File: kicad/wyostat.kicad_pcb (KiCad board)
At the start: 2 copper layers, 75 parts, among them J1 PWR_In, J10 MOSI, J11 RST, J12 GND, J13 AC_IN, J14 ~RST, J15 AC_IN, J16 5V_SEL, J2 OUT1, J3 OUT2, J4 OUT3, J5 I2C_ext1, J6 MISO, J7 3V3, J8 SCK, J9 SPI, Q1 BT136-600, Q2 BT136-600, Q3 BT136-600, U1 MOC3063M, U2 MOC3063M, U3 MOC3063M, U4 Wemos-Lolin, U5 MAX17502FATB+T, U6 Converter_AC_DC

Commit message: kicad PCB, WIP
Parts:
- removed J14: ~RST, wyostat_fp:Pin_Header_Straight_1x01
- moved R16 143.6 mm to (38.7, 134.6), turned to 90 degrees
- moved R7 127.3 mm to (55.2, 120.7), turned to 90 degrees
- moved R3 122.3 mm to (36.2, 109.9), turned to 90 degrees
- moved R10 119.5 mm to (38.7, 124.5), turned to 90 degrees
- moved U3 116.5 mm to (47.0, 132.7), turned to 270 degrees
- moved R11 111.1 mm to (80.0, 122.6)
- moved R8 110.3 mm to (55.2, 124.5), turned to 90 degrees
- moved R9 109.9 mm to (36.2, 120.0), turned to 90 degrees
- moved J10 108.2 mm to (56.5, 85.7), turned to 270 degrees
- moved J11 105.9 mm to (46.4, 88.3), turned to 90 degrees
- moved C1 105.3 mm to (85.1, 112.4), turned to 90 degrees
- moved R13 104.5 mm to (55.2, 130.8), turned to 90 degrees
- moved C5 104.5 mm to (85.1, 132.7), turned to 90 degrees
- moved D1 103.3 mm to (38.7, 109.9), turned to 90 degrees
- moved JP1 96.6 mm to (36.2, 114.3), turned to 90 degrees
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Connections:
- J13 pad 1: Net-(F1-Pad2) -> Net-(D4-Pad3)
- J13 pad 2: Net-(D4-Pad3) -> Net-(F1-Pad2)
- U4 pad 1: Net-(U4-Pad1) -> (no net)
- U4 pad 11: Net-(U4-Pad11) -> (no net)
- U4 pad 12: Net-(U4-Pad12) -> (no net)
- U4 pad 20: Net-(U4-Pad20) -> (no net)
- U4 pad 21: Net-(U4-Pad21) -> (no net)
- U4 pad 22: Net-(U4-Pad22) -> (no net)
- U4 pad 23: Net-(U4-Pad23) -> (no net)
- U4 pad 26: Net-(U4-Pad26) -> (no net)
- U4 pad 5: Net-(U4-Pad5) -> (no net)
- U4 pad 6: Net-(U4-Pad6) -> (no net)
- U5 pad 7: Net-(U5-Pad7) -> (no net)
- U5 pad 8: Net-(J14-Pad1) -> (no net)

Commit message: layou, WIP
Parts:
- added JP4: GND, wyostat_fp:LED_0402, F.Cu at (71.0, 70.2)
- added SC1: SCREW, wyostat_fp:MountingHole_3.2mm_M3_Pad_Via, F.Cu at (36.8, 36.8)
- added SC2: SCREW, wyostat_fp:MountingHole_3.2mm_M3_Pad_Via, F.Cu at (125.7, 36.8)
- added SC3: SCREW, wyostat_fp:MountingHole_3.2mm_M3_Pad_Via, F.Cu at (36.8, 125.7)
- added SC4: SCREW, wyostat_fp:MountingHole_3.2mm_M3_Pad_Via, F.Cu at (125.7, 125.7)
- U1, U2, U3: footprint wyostat_fp:Optocoupler_6pin -> wyostat_fp:Optocoupler_6pin_smd
- U6: footprint wyostat_fp:Converter_AC_DC -> wyostat_fp:Converter_AC_DC_Eshion
- moved J16 68.3 mm to (50.8, 74.3), turned to 180 degrees
- moved S4 59.3 mm to (109.9, 46.4)
- moved S2 59.3 mm to (117.5, 38.7), turned to 270 degrees
- moved S3 55.7 mm to (117.5, 54.0), turned to 270 degrees
- moved S1 55.7 mm to (125.1, 46.4), turned to 270 degrees
- moved C9 36.4 mm to (85.7, 68.6), turned to 270 degrees
- moved U6 34.8 mm to (70.9, 118.2), turned to 180 degrees
- moved C13 34.6 mm to (70.9, 63.8), turned to 0 degrees
- moved C10 34.4 mm to (78.7, 68.6)
- moved D3 33.8 mm to (53.3, 99.7)
- moved R15 33.8 mm to (50.8, 99.7)
- moved C4 33.8 mm to (77.5, 92.1)
- moved C6 33.8 mm to (77.5, 102.2)
- moved D1 33.8 mm to (53.3, 79.4)
- moved D2 33.8 mm to (53.3, 89.5)
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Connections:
- net Net-(C10-Pad1) renamed /40VDC
- net Net-(C12-Pad1) renamed /VCC
- net Net-(C13-Pad1) renamed /SS
- net Net-(L1-Pad1) renamed /LX
- C1 pad 1: /OUT1 -> /LINE
- C11 pad 2: GND -> GNDREF
- C14 pad 2: GND -> GNDREF
- C2 pad 2: /NEUT -> /OUT1
- C3 pad 1: /OUT2 -> /LINE
- C4 pad 2: /NEUT -> /OUT2
- C5 pad 1: /OUT3 -> /LINE
- C6 pad 2: /NEUT -> /OUT3
- J13 pad 1: Net-(D4-Pad3) -> Net-(F1-Pad2)
- J13 pad 2: Net-(F1-Pad2) -> Net-(D4-Pad3)
- J2 pad 1: /LINE -> /OUT1
- J2 pad 2: /OUT1 -> /NEUT
- J3 pad 1: /LINE -> /OUT2
- J3 pad 2: /OUT2 -> /NEUT
- J4 pad 1: /LINE -> /OUT3
- J4 pad 2: /OUT3 -> /NEUT
- Q1 pad 1: /OUT1 -> /LINE
- Q1 pad 2: /NEUT -> /OUT1
- Q2 pad 1: /OUT2 -> /LINE
- Q2 pad 2: /NEUT -> /OUT2
- Q3 pad 1: /OUT3 -> /LINE
- Q3 pad 2: /NEUT -> /OUT3
- R11 pad 1: /NEUT -> /OUT2
- R12 pad 1: /NEUT -> /OUT2
- R14 pad 1: /OUT3 -> /LINE
- R17 pad 1: /NEUT -> /OUT3
- R18 pad 1: /NEUT -> /OUT3
- R2 pad 1: /OUT1 -> /LINE
- R5 pad 1: /NEUT -> /OUT1
- R6 pad 1: /NEUT -> /OUT1
- R8 pad 1: /OUT2 -> /LINE
- U4 pad 1: (no net) -> Net-(U4-Pad1)
- U4 pad 11: (no net) -> Net-(U4-Pad11)
- U4 pad 12: (no net) -> Net-(U4-Pad12)
- U4 pad 20: (no net) -> Net-(U4-Pad20)
- U4 pad 21: (no net) -> Net-(U4-Pad21)
- U4 pad 22: (no net) -> Net-(U4-Pad22)
- U4 pad 23: (no net) -> Net-(U4-Pad23)
- U4 pad 26: (no net) -> Net-(U4-Pad26)
- U4 pad 5: (no net) -> Net-(U4-Pad5)
- U4 pad 6: (no net) -> Net-(U4-Pad6)
- U5 pad 1: GND -> GNDREF
- U5 pad 7: (no net) -> Net-(U5-Pad7)
- U5 pad 8: (no net) -> /R
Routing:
- net GND: track 0.00 -> 29.8 mm
- net /40VDC: track 0.00 -> 26.1 mm
- net /3V3: track 0.00 -> 21.1 mm
- net /5V_IN1: track 0.00 -> 18.6 mm, vias 0 -> 2
- net Net-(D4-Pad3): track 0.00 -> 14.6 mm
- net /SW_M: track 0.00 -> 8.99 mm
- net /SW_I: track 0.00 -> 8.99 mm
- net /SW_D: track 0.00 -> 8.99 mm
- net Net-(F1-Pad2): track 0.00 -> 7.41 mm
- net Net-(D4-Pad4): track 0.00 -> 6.28 mm
- net GNDREF: track 0.00 -> 5.98 mm
- net /SS: track 0.00 -> 5.34 mm
- net /SW_E: track 0.00 -> 2.99 mm
- net /LX: track 0.00 -> 2.80 mm
- net /5V: track 0.00 -> 2.54 mm
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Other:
- board outline added: 99.1 x 99.1 mm

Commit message: kicad PCB, track layout
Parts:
- removed C7: 100nF, wyostat_fp:C_0805
- removed J10: MOSI, wyostat_fp:Pin_Header_Straight_1x01
- removed J11: RST, wyostat_fp:Pin_Header_Straight_1x01
- removed J12: GND, wyostat_fp:Pin_Header_Straight_1x01
- removed J6: MISO, wyostat_fp:Pin_Header_Straight_1x01
- removed J7: 3V3, wyostat_fp:Pin_Header_Straight_1x01
- removed J8: SCK, wyostat_fp:Pin_Header_Straight_1x01
- removed J9: SPI, wyostat_fp:Pin_Header_Straight_2x03
- moved C13 7.37 mm to (63.5, 63.9), turned to 180 degrees
- moved JP4 6.83 mm to (72.1, 63.5)
- moved R12 5.43 mm to (71.1, 88.9), turned to 180 degrees
- moved R17 5.43 mm to (71.1, 99.1), turned to 180 degrees
- moved R5 5.43 mm to (71.1, 78.7), turned to 180 degrees
- moved R1 2.29 mm to (71.1, 81.9), turned to 180 degrees
- moved R13 2.29 mm to (71.1, 102.2), turned to 180 degrees
- moved R7 2.29 mm to (71.1, 92.1), turned to 180 degrees
- moved C8 2.08 mm to (40.0, 52.7)
- moved R11 2.01 mm to (95.2, 90.2), turned to 90 degrees
- moved R18 2.01 mm to (95.2, 100.3), turned to 90 degrees
- moved R6 2.01 mm to (95.2, 80.0), turned to 90 degrees
- moved J5 1.90 mm to (36.8, 50.2)
- moved R2 1.80 mm to (71.1, 85.1), turned to 180 degrees
- moved R14 1.80 mm to (71.1, 105.4), turned to 180 degrees
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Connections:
- C11 pad 2: GNDREF -> GND
- C14 pad 2: GNDREF -> GND
- JP4 pad 2: GNDREF -> GND
- U1 pad 3: Net-(U1-Pad3) -> (no net)
- U1 pad 5: Net-(U1-Pad5) -> (no net)
- U2 pad 3: Net-(U2-Pad3) -> (no net)
- U2 pad 5: Net-(U2-Pad5) -> (no net)
- U3 pad 3: Net-(U3-Pad3) -> (no net)
- U3 pad 5: Net-(U3-Pad5) -> (no net)
- U4 pad 1: Net-(U4-Pad1) -> (no net)
- U4 pad 11: Net-(U4-Pad11) -> (no net)
- U4 pad 12: Net-(U4-Pad12) -> (no net)
- U4 pad 2: /IN1 -> /IN3
- U4 pad 20: Net-(U4-Pad20) -> (no net)
- U4 pad 21: Net-(U4-Pad21) -> (no net)
- U4 pad 22: Net-(U4-Pad22) -> (no net)
- U4 pad 23: Net-(U4-Pad23) -> (no net)
- U4 pad 24: /IN3 -> /IN1
- U4 pad 26: Net-(U4-Pad26) -> (no net)
- U4 pad 5: Net-(U4-Pad5) -> (no net)
- U4 pad 6: Net-(U4-Pad6) -> (no net)
- U5 pad 1: GNDREF -> GND
- U5 pad 7: Net-(U5-Pad7) -> (no net)
- U5 pad 8: /R -> (no net)
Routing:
- net /3V3: track 21.1 -> 180.6 mm
- net /LINE: track 0.00 -> 130.0 mm, vias 0 -> 3
- net GND: track 29.8 -> 129.3 mm, vias 0 -> 26
- net /IN3: track 0.00 -> 96.5 mm
- net /SW_E: track 2.99 -> 85.8 mm
- net /SW_D: track 8.99 -> 80.0 mm
- net /5V: track 2.54 -> 67.4 mm
- net /SW_I: track 8.99 -> 66.1 mm
- net /SW_M: track 8.99 -> 64.0 mm
- net /5V_IN2: track 0.00 -> 43.6 mm
- net /NEUT: track 0.00 -> 39.7 mm
- net /IN2: track 0.00 -> 39.6 mm
- net Net-(Q2-Pad3): track 0.00 -> 39.1 mm
- net Net-(Q3-Pad3): track 0.00 -> 39.1 mm
- net Net-(Q1-Pad3): track 0.00 -> 39.1 mm
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- added copper zone on F.Cu, net /40VDC
- added copper zone on F.Cu, net /5V_IN1
- added copper zone on F.Cu, net /LX
- added copper zone on B.Cu, net GND
- added copper zone on F.Cu, net GND
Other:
- net class 10mil added: clearance 0.2032, trace_width 0.254, via_dia 0.8128, via_drill 0.4064
- net class 15mil added: clearance 0.2032, trace_width 0.381, via_dia 0.8128, via_drill 0.4064
- net class 20mil added: clearance 0.2032, trace_width 0.508, via_dia 0.8128, via_drill 0.4064
- net class 30mil added: clearance 0.2032, trace_width 0.762, via_dia 0.8128, via_drill 0.4064
- net class 40mil added: clearance 0.2032, trace_width 1.016, via_dia 0.8128, via_drill 0.4064
- net class Default: clearance 0.2 -> 0.2032; trace_width 0.25 -> 0.254; via_dia 0.8 -> 0.8128; via_drill 0.4 -> 0.4064
- rule trace_clearance: 0.2 -> 0.2032

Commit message: initial board layout
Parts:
- removed F2: Polyfuse, wyostat_fp:Fuse_SMD2920
- removed J15: AC_IN, wyostat_fp:TerminalBlock_Pheonix_MPT-2.54mm_2pol
- added BT1: Batt_RTC, wyostat_fp:CR2032_SMD2, F.Cu at (42.5, 81.3)
- added C15: 4.7uF, wyostat_fp:C_0805, F.Cu at (95.9, 73.4)
- added C7: 100nF, wyostat_fp:C_0805, F.Cu at (40.0, 52.7)
- added D5: CDSOD323-T05L, Diodes_SMD:D_SOD-323_HandSoldering, F.Cu at (99.7, 74.3)
- added L2: 330E, wyostat_fp:R_0805, F.Cu at (99.7, 72.4)
- added L4: 330E, wyostat_fp:R_0805, F.Cu at (99.7, 64.8)
- added R23: 0E, wyostat_fp:R_0805, F.Cu at (99.7, 70.5)
- added R24: 0E, wyostat_fp:R_0805, F.Cu at (99.7, 68.6)
- added R25: 0E, wyostat_fp:R_0805, F.Cu at (99.7, 66.7)
- added R26: 10k, wyostat_fp:R_0805, F.Cu at (54.6, 76.2)
- added R27: 10k, wyostat_fp:R_0805, F.Cu at (54.6, 73.0)
- added R28: 4K7, wyostat_fp:R_0805, F.Cu at (54.6, 64.1)
- added R29: 4K7, wyostat_fp:R_0805, F.Cu at (54.6, 66.0)
- added TP1: ~RST, wyostat_fp:Pin_Header_Straight_1x01, F.Cu at (76.2, 68.6)
- added TP2: SQR, wyostat_fp:Pin_Header_Straight_1x01, F.Cu at (73.7, 68.6)
- added TP3: 32kHz, wyostat_fp:Pin_Header_Straight_1x01, F.Cu at (71.1, 68.6)
- J1: value PWR_In -> 24VAC IN
- J13: value AC_IN -> USB_microAB; footprint wyostat_fp:TerminalBlock_Pheonix_MPT-2.54mm_2pol -> wyostat_fp:USB_Micro-B_Molex-105017-0001
- J16: value 5V_SEL -> EXT<OFF>USB
- R14, R2, R8: value 470 -> 0E
- U6: value Converter_AC_DC -> DS3231N; footprint wyostat_fp:Converter_AC_DC_Eshion -> wyostat_fp:DS3231
- moved U6 50.4 mm to (62.2, 68.6), turned to 0 degrees
- moved J16 41.3 mm to (92.1, 72.4), turned to 270 degrees
- moved J1 27.9 mm to (106.7, 84.5)
- moved C8 21.6 mm to (54.6, 68.6), turned to 0 degrees
- moved R3 14.6 mm to (50.8, 94.0)
- moved JP1 13.3 mm to (50.8, 97.2)
- moved C10 12.7 mm to (78.7, 81.3)
- moved C11 12.7 mm to (71.0, 82.9)
- moved C12 12.7 mm to (70.9, 78.5)
- moved C13 12.7 mm to (63.5, 76.6)
- moved C14 12.7 mm to (67.3, 82.9)
- moved C3 12.7 mm to (99.7, 104.8)
- moved C4 12.7 mm to (77.5, 104.8)
- moved C5 12.7 mm to (99.7, 114.9)
- moved C6 12.7 mm to (77.5, 114.9)
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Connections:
- C1 pad 1: /LINE -> /24Vac-H
- C3 pad 1: /LINE -> /24Vac-H
- C5 pad 1: /LINE -> /24Vac-H
- C8 pad 1: /3V3 -> /rtc_ds3231/BAT
- D4 pad 3: Net-(D4-Pad3) -> /24Vac-C
- F1 pad 2: Net-(F1-Pad2) -> /24Vac-H
- J1 pad 1: /LINE -> /24Vac-H
- J1 pad 2: /NEUT -> /24Vac-C
- J13 pad 1: Net-(F1-Pad2) -> /USB+
- J13 pad 2: Net-(D4-Pad3) -> /D-
- J2 pad 2: /NEUT -> /24Vac-C
- J3 pad 2: /NEUT -> /24Vac-C
- J4 pad 2: /NEUT -> /24Vac-C
- Q1 pad 1: /LINE -> /24Vac-H
- Q2 pad 1: /LINE -> /24Vac-H
- Q3 pad 1: /LINE -> /24Vac-H
- R14 pad 1: /LINE -> /24Vac-H
- R2 pad 1: /LINE -> /24Vac-H
- R8 pad 1: /LINE -> /24Vac-H
- U6 pad 1: Net-(F2-Pad1) -> /rtc_ds3231/32kHz
- U6 pad 2: Net-(J15-Pad2) -> /3V3
- U6 pad 3: /5V_IN2 -> /rtc_ds3231/SQR
- U6 pad 4: GND -> /rtc_ds3231/RESET
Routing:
- net GND: track 129.3 -> 295.8 mm, vias 26 -> 32
- net /24Vac-H: track 0.00 -> 134.2 mm, vias 0 -> 4
- net /LINE: track 130.0 -> 0.00 mm, vias 3 -> 0
- net /3V3: track 180.6 -> 237.0 mm
- net /24Vac-C: track 0.00 -> 54.1 mm
- net /rtc_ds3231/BAT: track 0.00 -> 53.1 mm, vias 0 -> 3
- net /SCL: track 27.0 -> 71.6 mm, vias 0 -> 1
- net /SDA: track 31.2 -> 73.0 mm
- net /NEUT: track 39.7 -> 0.00 mm
- net /5V_IN2: track 43.6 -> 6.68 mm
- net /rtc_ds3231/SQR: track 0.00 -> 24.3 mm
- net Net-(J15-Pad2): track 24.0 -> 0.00 mm
- net Net-(J13-PadS1): track 0.00 -> 23.8 mm
- net /IN1: track 29.6 -> 52.5 mm, vias 0 -> 1
- net /5V_IN1: track 28.0 -> 47.4 mm, vias 2 -> 4
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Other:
- outline, holes or cut-outs redrawn
- board text added: "H | C"
- board text added: "SCL SDA 3V3 GND"

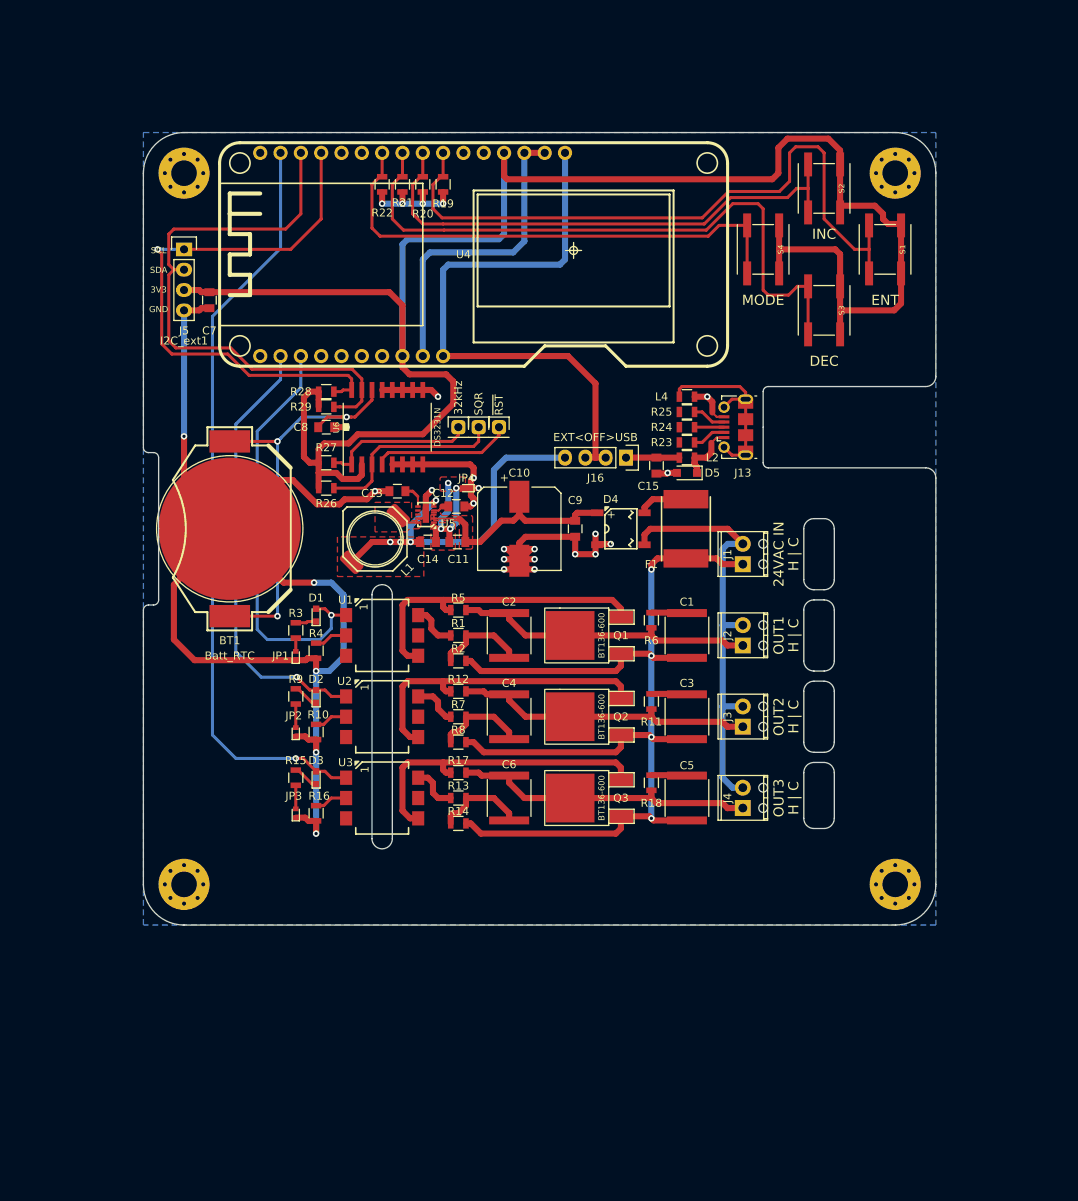
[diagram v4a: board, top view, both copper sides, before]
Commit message: adding pads for spring contacts
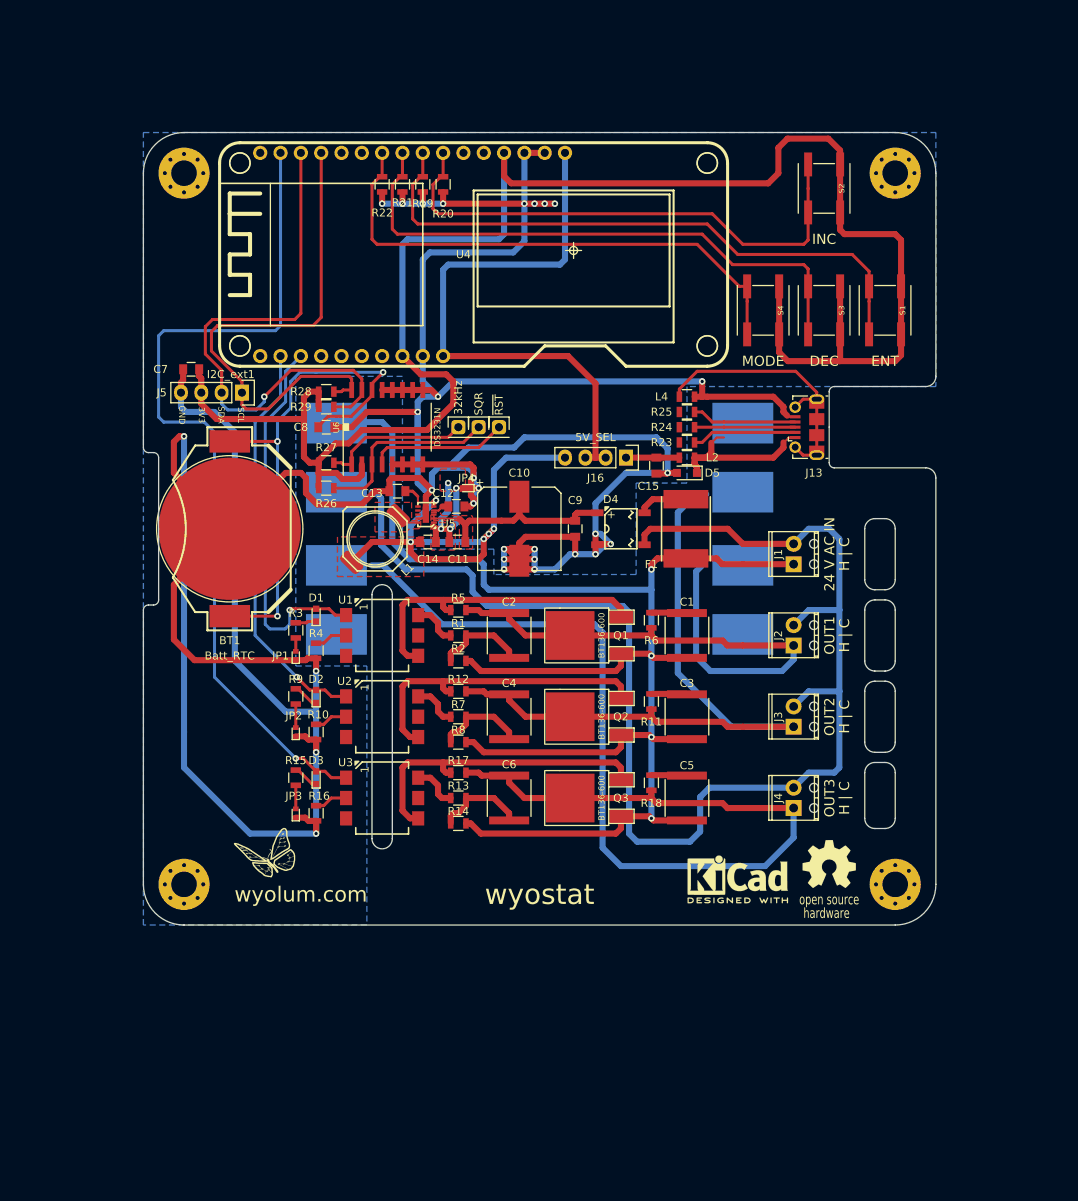
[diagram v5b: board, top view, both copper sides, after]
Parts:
- added G1: LOGO_WL, wyostat_fp:Logo-WL3, F.Cu at (41.9, 118.1)
- added G2: OSHW, wyostat_fp:OSHW_6mm, F.Cu at (117.5, 123.2)
- added G3: KiCad, wyostat_fp:KiCad-Logo2_6mm_SilkScreen, F.Cu at (106.0, 125.1)
- added REF**: pad_rect_smd, wyostat_fp:pad_rect_smd, B.Cu at (55.9, 94.5)
- added REF**: pad_rect_smd, wyostat_fp:pad_rect_smd, B.Cu at (55.9, 85.9)
- added REF**: pad_rect_smd, wyostat_fp:pad_rect_smd, B.Cu at (106.7, 94.5)
- added REF**: pad_rect_smd, wyostat_fp:pad_rect_smd, B.Cu at (106.7, 68.1)
- added REF**: pad_rect_smd, wyostat_fp:pad_rect_smd, B.Cu at (106.7, 85.9)
- added REF**: pad_rect_smd, wyostat_fp:pad_rect_smd, B.Cu at (106.7, 76.7)
- added REF**: pad_rect_smd, wyostat_fp:pad_rect_smd, B.Cu at (55.9, 76.7)
- added REF**: pad_rect_smd, wyostat_fp:pad_rect_smd, B.Cu at (55.9, 68.1)
- C10: footprint Capacitors_SMD:CP_Elec_10x10 -> wyostat_fp:CP_Elec_10x10
- J1: value 24VAC IN -> 24 V AC IN
- J16: value EXT<OFF>USB -> 5V_SEL
- Q1, Q2, Q3: footprint SMD_Packages:DPAK-2 -> wyostat_fp:DPAK-2
- moved J5 14.5 mm to (40.3, 64.3), turned to 270 degrees
- moved C7 8.93 mm to (37.7, 61.3), turned to 180 degrees
- moved J13 8.89 mm to (115.6, 68.6)
- moved S1 7.62 mm to (124.5, 54.0)
- moved S4 7.62 mm to (109.2, 54.0)
- moved J1 6.35 mm to (113.0, 84.5)
- moved J2 6.35 mm to (113.0, 94.6)
- moved J3 6.35 mm to (113.0, 104.8)
- moved J4 6.35 mm to (113.0, 114.9)
- moved R19 2.54 mm to (66.7, 38.2)
- moved R20 2.54 mm to (69.2, 38.2)
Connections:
- R23 pad 1: (no net) -> /USB_D-
- R24 pad 1: (no net) -> /USB_D+
- R25 pad 1: (no net) -> /USB_ID
- U1 pad 3: (no net) -> Net-(U1-Pad3)
- U1 pad 5: (no net) -> Net-(U1-Pad5)
- U2 pad 3: (no net) -> Net-(U2-Pad3)
- U2 pad 5: (no net) -> Net-(U2-Pad5)
- U3 pad 3: (no net) -> Net-(U3-Pad3)
- U3 pad 5: (no net) -> Net-(U3-Pad5)
- U4 pad 1: (no net) -> Net-(U4-Pad1)
- U4 pad 10: /SW_E -> /SW_I
- U4 pad 11: (no net) -> Net-(U4-Pad11)
- U4 pad 12: (no net) -> Net-(U4-Pad12)
- U4 pad 20: (no net) -> Net-(U4-Pad20)
- U4 pad 21: (no net) -> Net-(U4-Pad21)
- U4 pad 22: (no net) -> Net-(U4-Pad22)
- U4 pad 23: (no net) -> Net-(U4-Pad23)
- U4 pad 26: (no net) -> Net-(U4-Pad26)
- U4 pad 5: (no net) -> Net-(U4-Pad5)
- U4 pad 6: (no net) -> Net-(U4-Pad6)
- U4 pad 9: /SW_I -> /SW_E
- U5 pad 7: (no net) -> Net-(U5-Pad7)
- U5 pad 8: (no net) -> /R
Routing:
- net GND: track 295.8 -> 542.8 mm, vias 32 -> 34
- net /24Vac-C: track 54.1 -> 173.3 mm
- net /OUT3: track 37.9 -> 133.6 mm
- net /24Vac-H: track 134.2 -> 198.2 mm
- net /OUT2: track 37.9 -> 86.0 mm
- net /OUT1: track 37.8 -> 71.2 mm
- net /USB+: track 7.47 -> 21.5 mm
- net /rtc_ds3231/BAT: track 53.1 -> 65.9 mm
- net /IN3: track 95.2 -> 107.6 mm
- net /5V_IN1: track 47.4 -> 59.7 mm, vias 4 -> 5
- net /3V3: track 237.0 -> 226.2 mm
- net Net-(J13-PadS1): track 23.8 -> 34.2 mm
- net /D-: track 4.20 -> 13.3 mm
- net /ID: track 4.20 -> 13.1 mm
- net /D+: track 3.69 -> 12.6 mm
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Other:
- outline, holes or cut-outs redrawn
- board text added: "C"
- board text added: "H"
- board text added: "OUT1"
- board text added: "OUT2"
- board text added: "hardware"
- board text added: "open source"
- board text added: "wyolum.com"
- board text added: "wyostat"
